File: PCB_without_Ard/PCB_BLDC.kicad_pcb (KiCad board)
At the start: 2 copper layers, 158.8 x 92.7 mm, 72 parts, among them J1 Ground Terminal, J2 Conn_01x03, J3 Conn_01x05, J4 Conn_01x02, J5 Conn_01x04, J6 Conn_01x04, J7 Conn_01x04, J8 Power Terminal, J9 Conn_01x02, Q1 IRF4905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

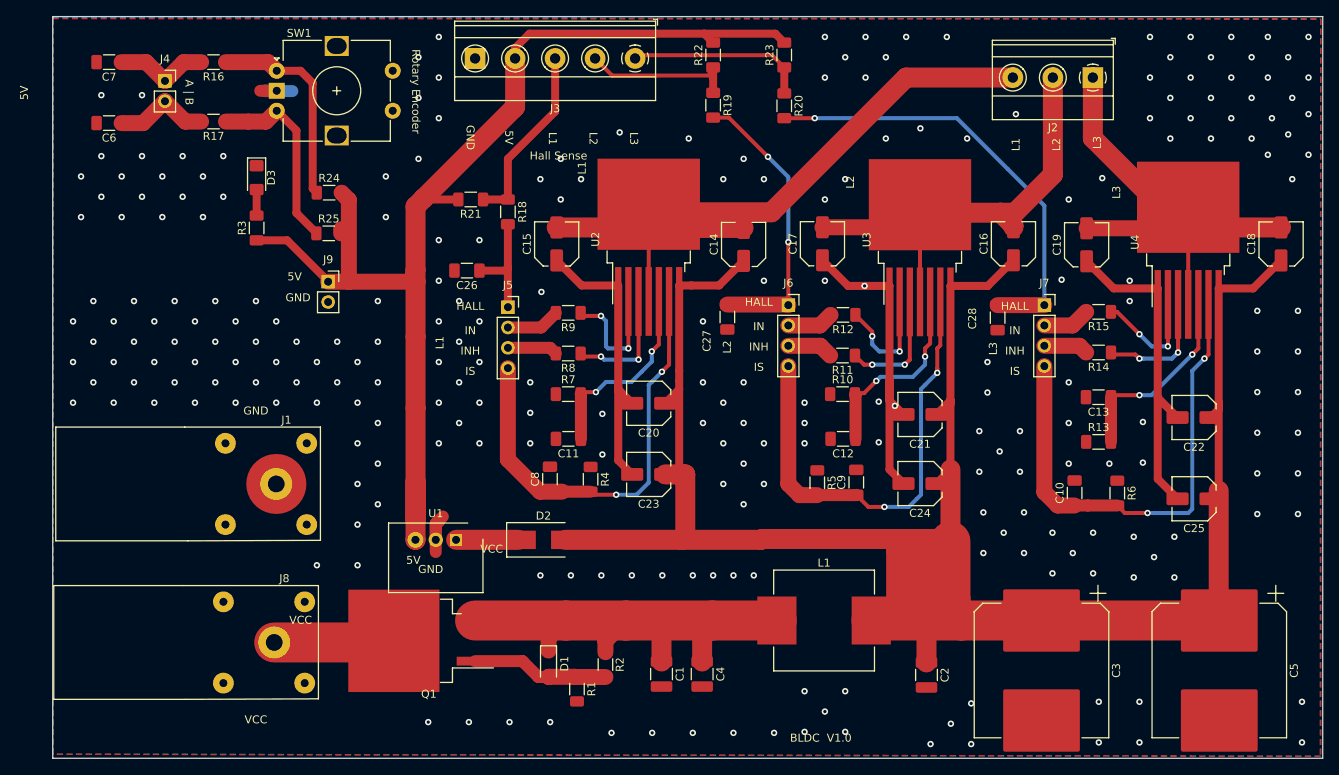
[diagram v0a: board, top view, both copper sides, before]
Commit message: Remove RC-Filter for Hall Sensors
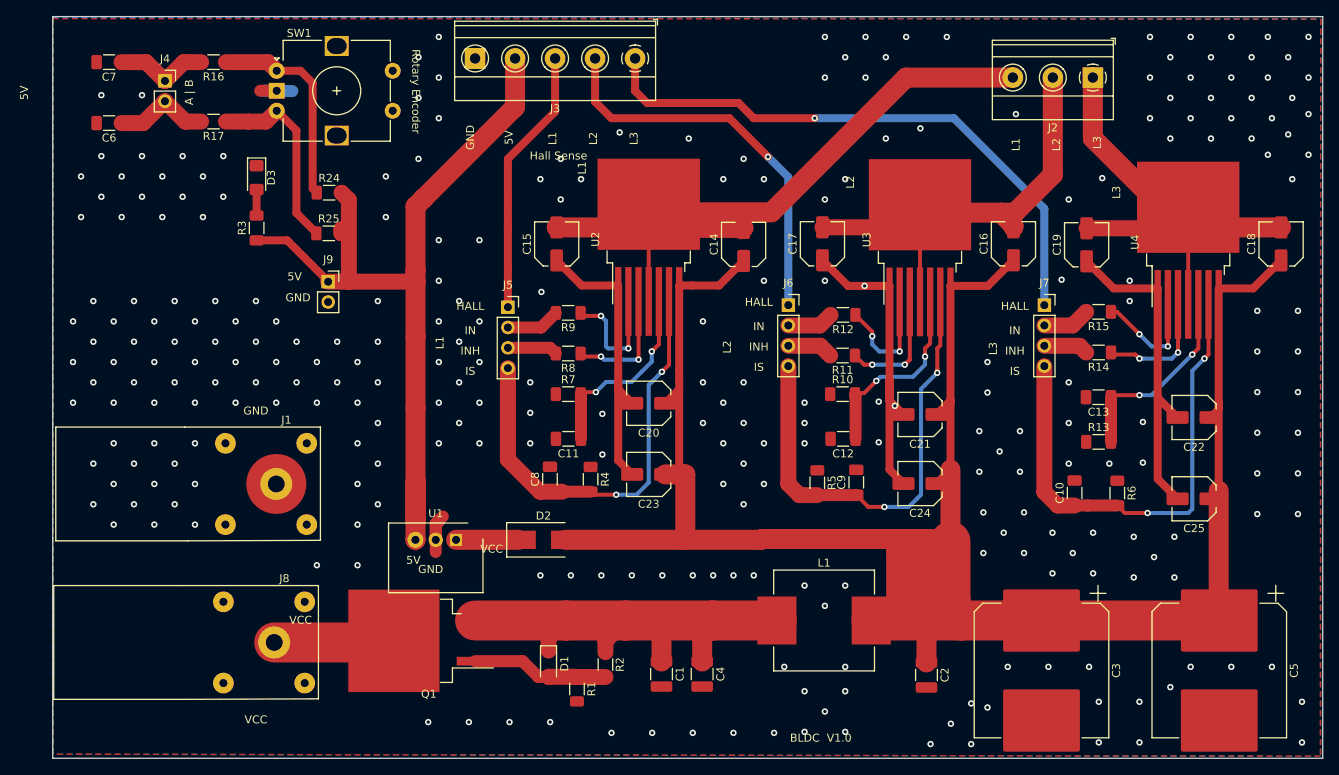
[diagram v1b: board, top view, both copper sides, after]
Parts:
- removed C26, C27, C28: 1nF, Capacitor_SMD:C_1206_3216Metric_Pad1.33x1.80mm_HandSolder
- removed R18, R19, R20, R21, R22, R23: 10k, Resistor_SMD:R_1206_3216Metric_Pad1.30x1.75mm_HandSolder
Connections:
- J1 pad 2: GND -> (no net)
- J5 pad 1: Net-(C26-Pad1) -> /L1_Sense
- J6 pad 1: Net-(C27-Pad1) -> /L2_Sense
- J7 pad 1: Net-(C28-Pad1) -> /L3_Sense
- J8 pad 2: GND -> (no net)
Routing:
- net Net-(C28-Pad1): track 55.3 -> 0.00 mm, vias 1 -> 0
- net /L3_Sense: track 22.6 -> 73.4 mm, vias 0 -> 1
- net /VCC_5V: track 147.8 -> 105.7 mm
- net Net-(C27-Pad1): track 36.1 -> 0.00 mm, vias 2 -> 0
- net /L2_Sense: track 19.3 -> 49.5 mm, vias 0 -> 1
- net Net-(C26-Pad1): track 14.0 -> 0.00 mm
- net /L1_Sense: track 23.2 -> 34.0 mm
- net GND: vias 251 -> 278
